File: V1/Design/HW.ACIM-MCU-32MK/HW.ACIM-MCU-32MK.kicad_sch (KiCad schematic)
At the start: 23 parts, among them J1 HEADER 2x15POS, J2 HEADER 2x15POS, U1 MIPS 32-bit DSC, U2 12MHz

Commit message: HW.ACIM-MCU-32MK Rev0.0
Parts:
- added TP1: GND, SAMPI:TP1MM, symbol Liem:TESTPOINT
- added TP2: 3V3, SAMPI:TP1MM, symbol Liem:TESTPOINT
- added TP3: AGND, SAMPI:TP1MM, symbol Liem:TESTPOINT
- added TP4: AVDD, SAMPI:TP1MM, symbol Liem:TESTPOINT
- C1, C19, C20: MFT (none) -> Murata; MNP (none) -> GRM1555C1H220JA01D
- C13, C22, C24, C26, C28: MNP GRM155C80J106ME11D -> GRM155C80J106ME11D
- D1: MFT (none) -> Harvatek; MNP (none) -> B1931NG--20D001114U1930
- D2: MFT (none) -> Harvatek; MNP (none) -> B1931URO-20D000114U1930
- J1, J2: MFT Hirose Electric Co Ltd -> Amphenol; MNP DF40GB-30DP-0.4V(51) -> 10152265-1301HF
- R1, R2: MFT (none) -> Yageo; MNP (none) -> RC0402JR-071KL
- R3: MFT (none) -> Yageo; MNP (none) -> RC0402JR-0710KL
- U2: MFT Abracon LLC -> Abracon
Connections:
- net +3V3: now also TP2.1
- net AGND: now also TP3.1
- net AVDD: now also TP4.1
- net GND: now also TP1.1
- net CTS2 renamed DV_CTS
- net IO00 renamed ~{BUTTON}
- net IO01 renamed IO1
- net IO1: now also U1.24 (AN11/CVD11/C1IN2-/FLT4/PMA12/RC11); no longer U1.28 (AN13/CVD13/C3IN2-/FLT6/SCL4/PMA10/RE13)
- net IO02 renamed IO2
- net IO2: now also U1.22 (OA3IN-/AN7/CVD7/C3IN1-/C4IN1-/RPC1/PMA7/RC1); no longer U1.27 (AN12/CVD12/C2IN2-/C5IN2-/SDA4/FLT5/PMA11/RE12)
- net IO03 renamed PWR_RELAY
- net PWR_RELAY: now also U1.62 (RPB12/PWM2H/PMD2/RB12); no longer U1.24 (AN11/CVD11/C1IN2-/FLT4/PMA12/RC11)
- net IO04 renamed DEV_RELAY
- net DEV_RELAY: now also U1.17 (PGC1/OA1IN+/AN4/C1IN1+/C1IN3-/C2IN3-/RPB2/RB2); no longer U1.22 (OA3IN-/AN7/CVD7/C3IN1-/C4IN1-/RPC1/PMA7/RC1)
- net IO05 renamed SCL
- net SCL: now also U1.28 (AN13/CVD13/C3IN2-/FLT6/SCL4/PMA10/RE13); no longer U1.63 (RPB13/PWM8H/PWM2L/CTPLS/PMD3/RB13)
- net IO06 renamed SDA
- net SDA: now also U1.27 (AN12/CVD12/C2IN2-/C5IN2-/SDA4/FLT5/PMA11/RE12); no longer U1.62 (RPB12/PWM2H/PMD2/RB12)
- net IO07 renamed SCK
- net SCK: now also J1.15; no longer J1.13
- net IO08 renamed SDI
- net SDI: now also J1.16; no longer J1.14
- removed net IO09: J1.15, U1.17 (PGC1/OA1IN+/AN4/C1IN1+/C1IN3-/C2IN3-/RPB2/RB2)
- net IO10 renamed ~{CS}
- net ~{CS}: now also J1.13; no longer J1.16
- net RTS2 renamed DV_RTS
- net RXD1 renamed DB_RXD
- net RXD2 renamed DV_RXD
- net TXD1 renamed DB_TXD
- net TXD2 renamed DV_TXD
- new net SDO: J1.14, U1.63 (RPB13/PWM8H/PWM2L/CTPLS/PMD3/RB13)
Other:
- title: MCU PLUG-IN MODULE (PIM) -> PIC32MK MCU PLUG-IN MODULE (PIM)
- moved on the sheet: C1, C10, C12, C13, C19, C20, C21, C22, C23, C24, C25, C26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

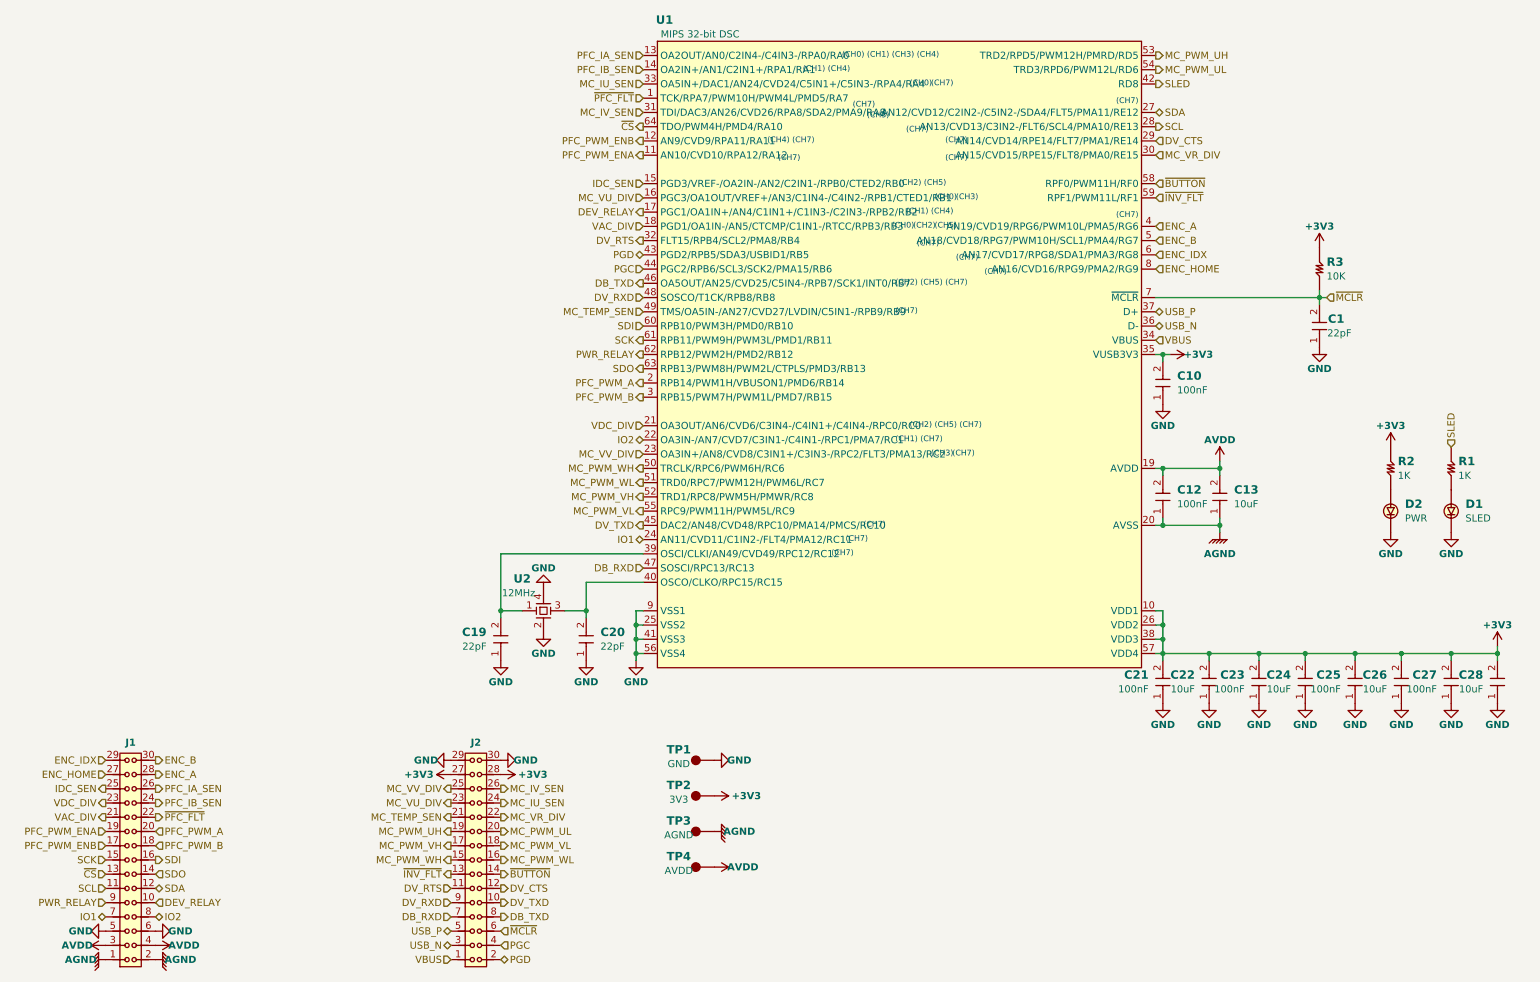
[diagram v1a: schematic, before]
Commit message: HW.ACIM-MCU-32MK update net name
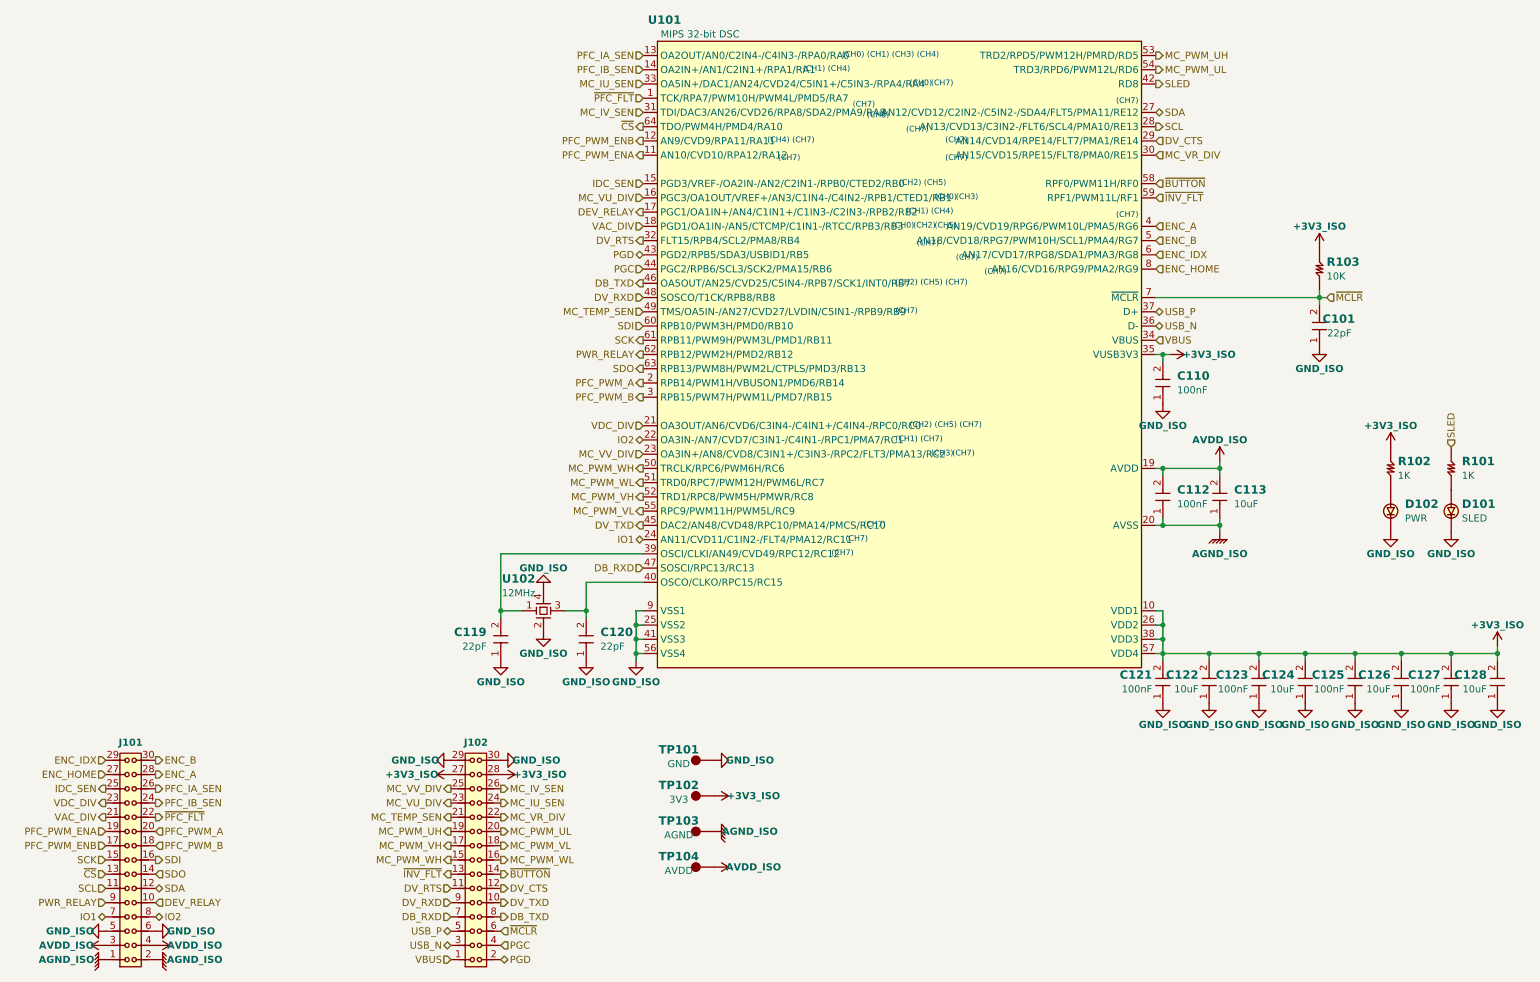
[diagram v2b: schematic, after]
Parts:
- renumbered C1 to C101, C10 to C110, C12 to C112, C13 to C113, C19 to C119, C20 to C120, C21 to C121, C22 to C122, C23 to C123, C24 to C124, C25 to C125, C26 to C126, C27 to C127, C28 to C128, D1 to D101, D2 to D102, J1 to J101, J2 to J102, R1 to R101, R2 to R102, R3 to R103, TP1 to TP101, TP2 to TP102, TP3 to TP103, TP4 to TP104, U1 to U101, U2 to U102
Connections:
- net +3V3 renamed +3V3_ISO
- net AGND renamed AGND_ISO
- net AVDD renamed AVDD_ISO
- net GND renamed GND_ISO
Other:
- company: TON DUC THANG UNIVERSITY -> (none)
- moved on the sheet: C119, C122, C124, C126, C128
